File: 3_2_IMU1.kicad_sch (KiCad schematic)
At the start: 3 parts, among them U701 LSM6DSO32TR

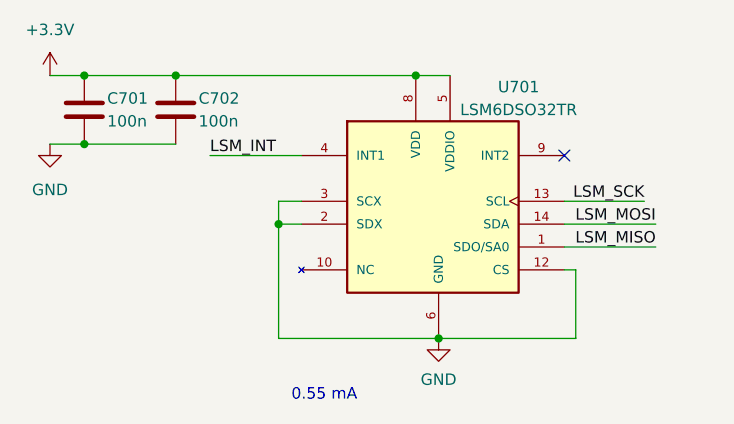
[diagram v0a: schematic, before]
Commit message: Finished restructuring schematic
Most components that were on page 3 are now in their own page
Added high-frequency 4.7 uF capacitor to servo power line
Continuity sensing on pyrochannels is multiplexed to one ADC on NAV.
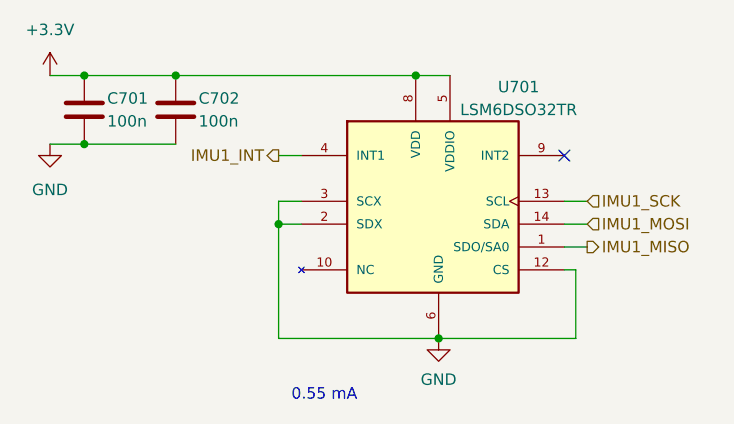
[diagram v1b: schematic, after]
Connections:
- net LSM_INT renamed IMU1_INT
- net LSM_MISO renamed IMU1_MISO
- net LSM_MOSI renamed IMU1_MOSI
- net LSM_SCK renamed IMU1_SCK
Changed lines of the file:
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@@
+	(wire
+		(pts
+			(xy 134.62 92.71) (xy 137.16 92.71)
+		)
+		(stroke
+			(width 0)
+			(type default)
+		)
+	)
+	(wire
+		(pts
+			(xy 166.37 100.33) (xy 168.91 100.33)
+		)
+		(stroke
+			(width 0)
+			(type default)
+		)
+	)
+	(wire
+		(pts
+			(xy 166.37 97.79) (xy 168.91 97.79)
+		)
+		(stroke
+			(width 0)
+			(type default)
+		)
+	)
 	(wire
 		(pts
@@
 	(wire
 		(pts
-			(xy 166.37 97.79) (xy 175.26 97.79)
-		)
-		(stroke
-			(width 0)
-			(type default)
-		)
-	)
-	(wire
-		(pts
 			(xy 113.03 91.44) (xy 123.19 91.44)
-		)
-		(stroke
-			(width 0)
-			(type default)
-		)
-	)
-	(wire
-		(pts
-			(xy 166.37 100.33) (xy 176.53 100.33)
 		)
 		(stroke
@@
 	(wire
 		(pts
-			(xy 127 92.71) (xy 137.16 92.71)
-		)
-		(stroke
-			(width 0)
-			(type default)
-		)
-	)
-	(wire
-		(pts
 			(xy 134.62 100.33) (xy 137.16 100.33)
 		)
@@
 		(pts
 			(xy 134.62 100.33) (xy 134.62 113.03)
-		)
-		(stroke
-			(width 0)
-			(type default)
-		)
-	)
-	(wire
-		(pts
-			(xy 166.37 102.87) (xy 176.53 102.87)
 		)
 		(stroke
@@
 	(wire
 		(pts
+			(xy 166.37 102.87) (xy 168.91 102.87)
+		)
+		(stroke
+			(width 0)
+			(type default)
+		)
+	)
+	(wire
+		(pts
 			(xy 113.03 83.82) (xy 123.19 83.82)
 		)
@@
 		)
 	)
-	(label "LSM_INT"
-		(at 127 92.71 0)
+	(hierarchical_label "IMU1_MOSI"
+		(shape input)
+		(at 168.91 100.33 0)
 		(effects
 			(font
 				(size 1.27 1.27)
 			)
-			(justify left bottom)
+			(justify left)
 		)
 	)
-	(label "LSM_MISO"
-		(at 176.53 102.87 180)
+	(hierarchical_label "IMU1_MISO"
+		(shape output)
+		(at 168.91 102.87 0)
 		(effects
 			(font
 				(size 1.27 1.27)
 			)
-			(justify right bottom)
+			(justify left)
 		)
 	)
-	(label "LSM_MOSI"
-		(at 176.53 100.33 180)
+	(hierarchical_label "IMU1_SCK"
+		(shape input)
+		(at 168.91 97.79 0)
 		(effects
 			(font
 				(size 1.27 1.27)
 			)
-			(justify right bottom)
+			(justify left)
 		)
 	)
-	(label "LSM_SCK"
-		(at 175.26 97.79 180)
+	(hierarchical_label "IMU1_INT"
+		(shape output)
+		(at 134.62 92.71 180)
 		(effects
 			(font
 				(size 1.27 1.27)
 			)
-			(justify right bottom)
+			(justify right)
 		)
 	)
